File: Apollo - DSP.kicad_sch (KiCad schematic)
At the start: 27 parts, among them J1 USB_C_Receptacle_USB2.0, U1 NCP115ASN330T2G, U2 USBLC6-2SC6, U3 NCP115ASN330T2G

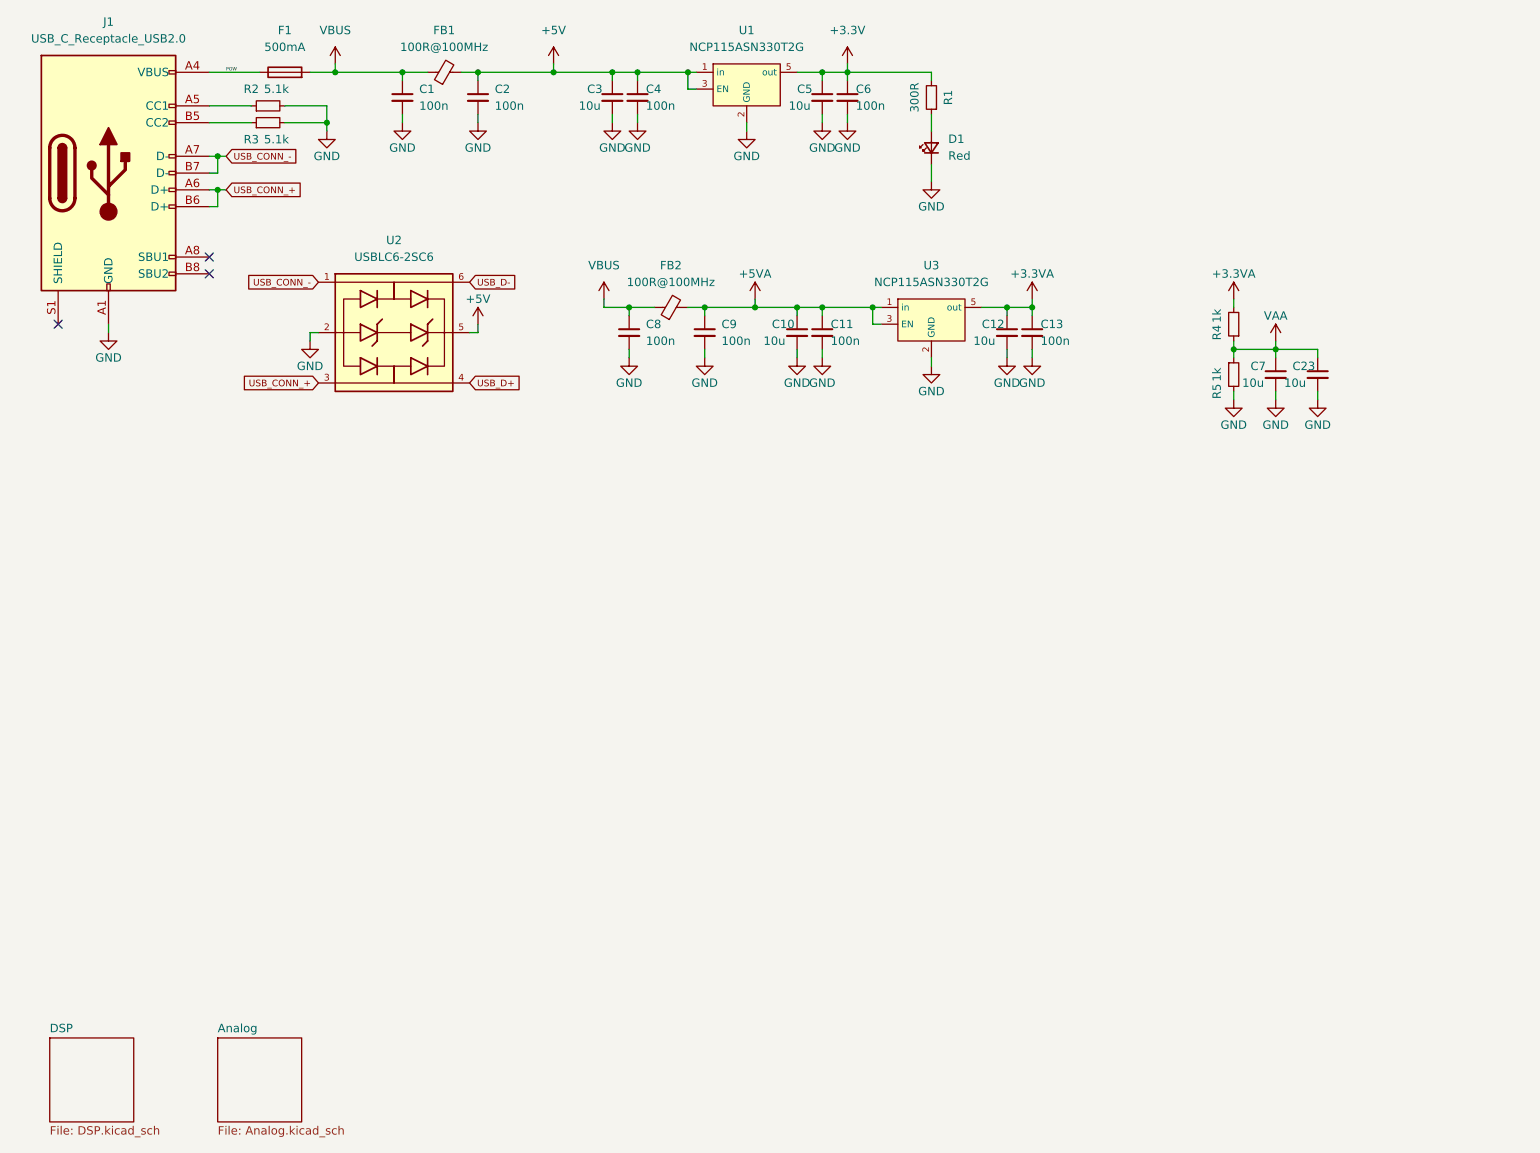
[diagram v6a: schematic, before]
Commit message: smaller mounting holes improved usb routing
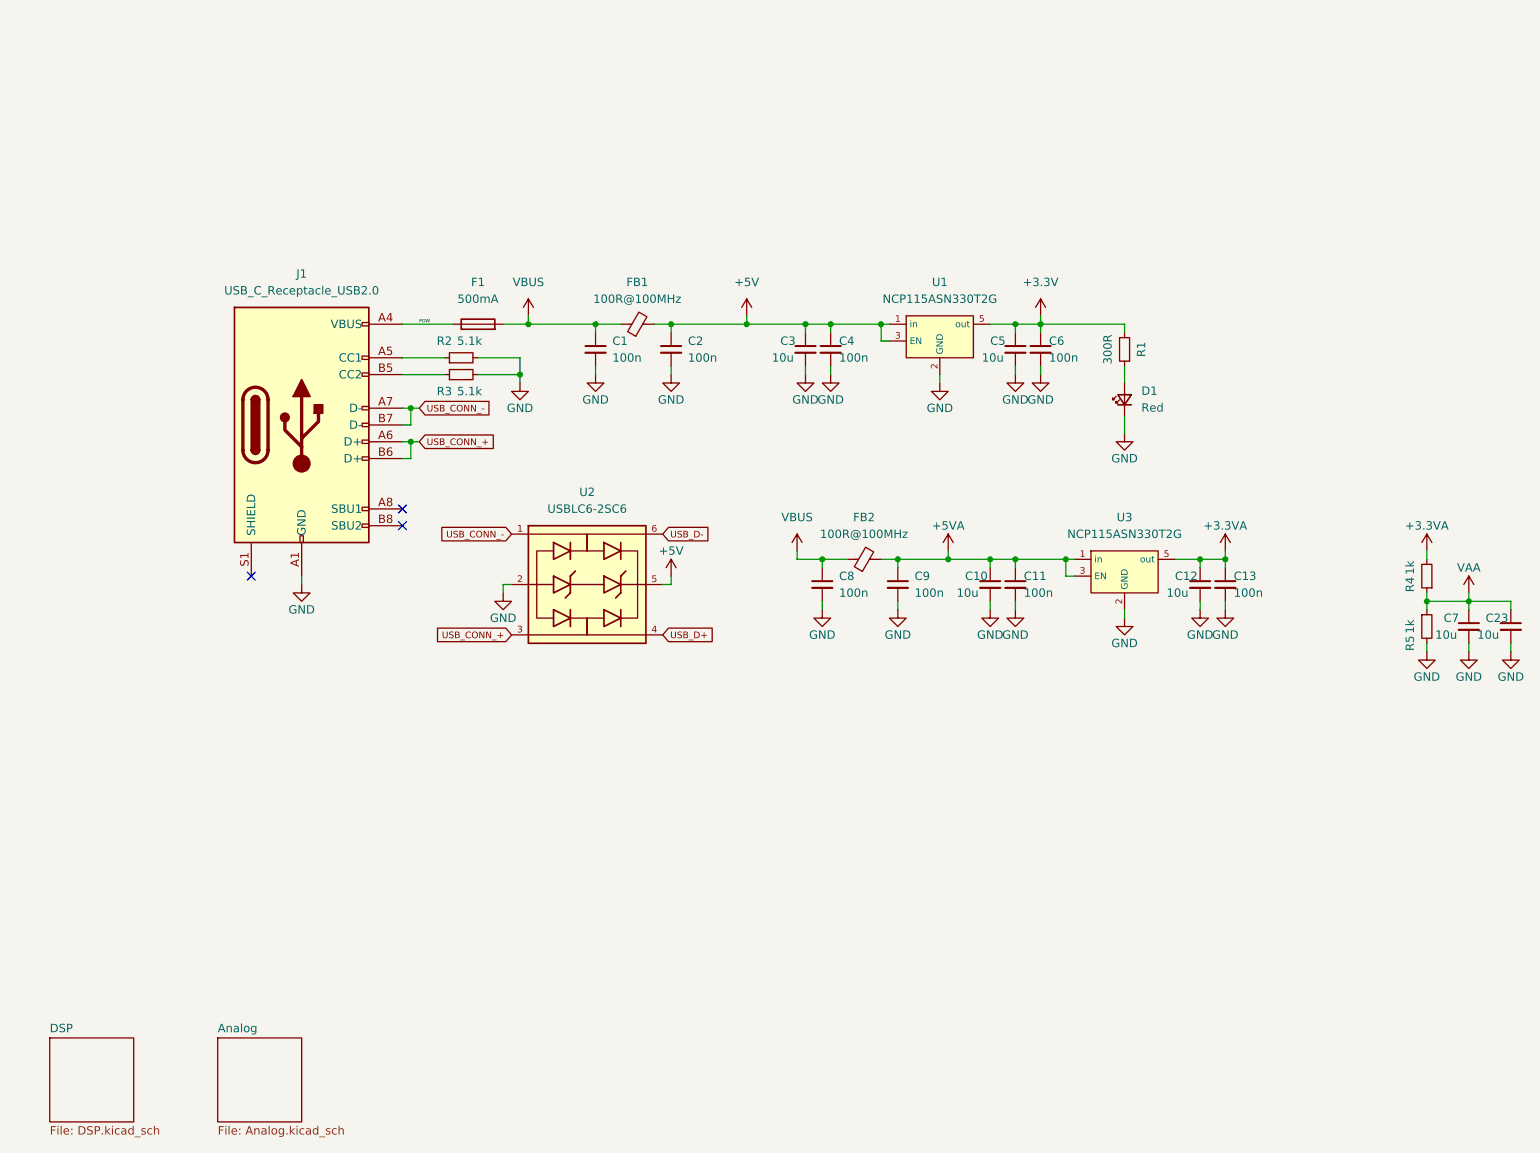
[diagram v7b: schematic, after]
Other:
- moved on the sheet: C1, C10, C11, C12, C13, C2, C23, C3, C4, C5, C6, C7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

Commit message: cleaned up the whole board
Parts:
- R4, R5: value 1k -> 5k1
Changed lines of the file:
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@@
   (symbol (lib_id "Device:R_Small") (at 233.68 107.95 180) (unit 1)
     (in_bom yes) (on_board yes) (dnp no)
-    (property "Reference" "R4" (at 231.14 109.22 90)
+    (property "Reference" "R4" (at 228.6 107.95 90)
       (effects (font (size 1.27 1.27)))
     )
-    (property "Value" "1k" (at 231.14 106.68 90)
+    (property "Value" "5k1" (at 231.14 107.95 90)
       (effects (font (size 1.27 1.27)))
     )
@@
   (symbol (lib_id "Device:R_Small") (at 233.68 115.57 0) (unit 1)
     (in_bom yes) (on_board yes) (dnp no)
-    (property "Reference" "R5" (at 231.14 118.11 90)
+    (property "Reference" "R5" (at 228.6 115.57 90)
       (effects (font (size 1.27 1.27)))
     )
-    (property "Value" "1k" (at 231.14 115.57 90)
+    (property "Value" "5k1" (at 231.14 115.57 90)
       (effects (font (size 1.27 1.27)))
     )
